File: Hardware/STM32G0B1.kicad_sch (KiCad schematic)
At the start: 20 parts, among them SW1 SW_Push, SW2 SW_Push, SW3 SW_Push, SW4 SW_Push, SW5 SW_Push

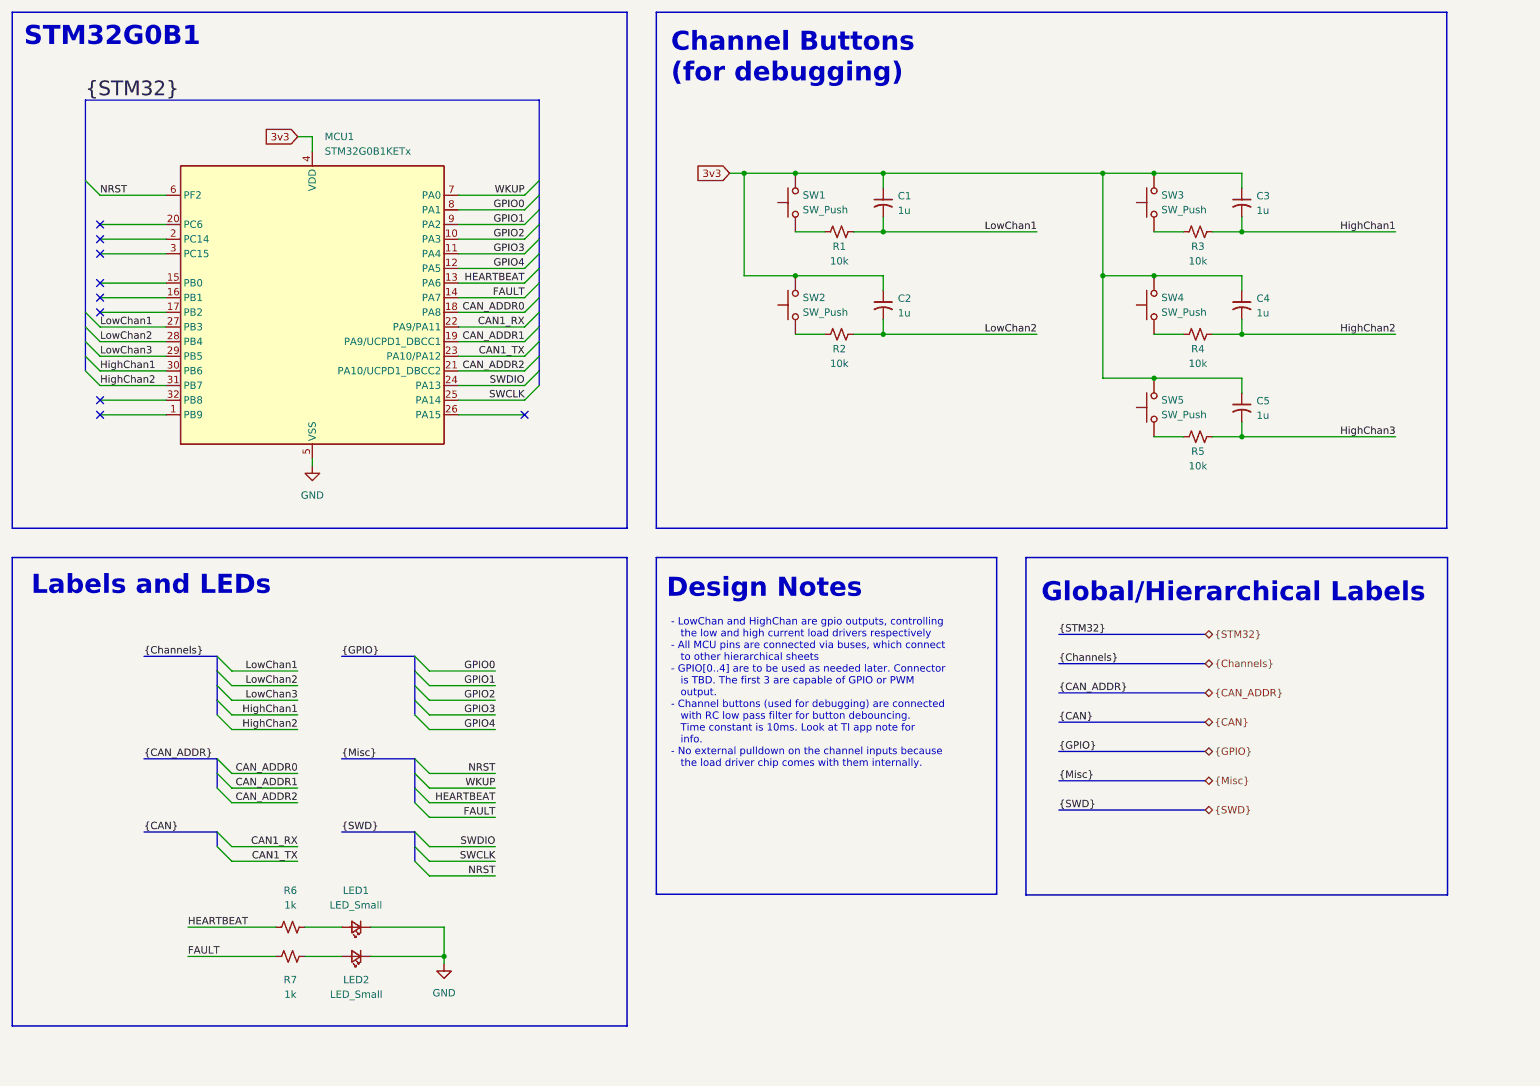
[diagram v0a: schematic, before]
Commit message: Finished the ISOW1044 Schematic
- Ported over Kostadin's schematic

Co-authored-by: Kostadin Madjovski <155325994+bivein@users.noreply.github.com>
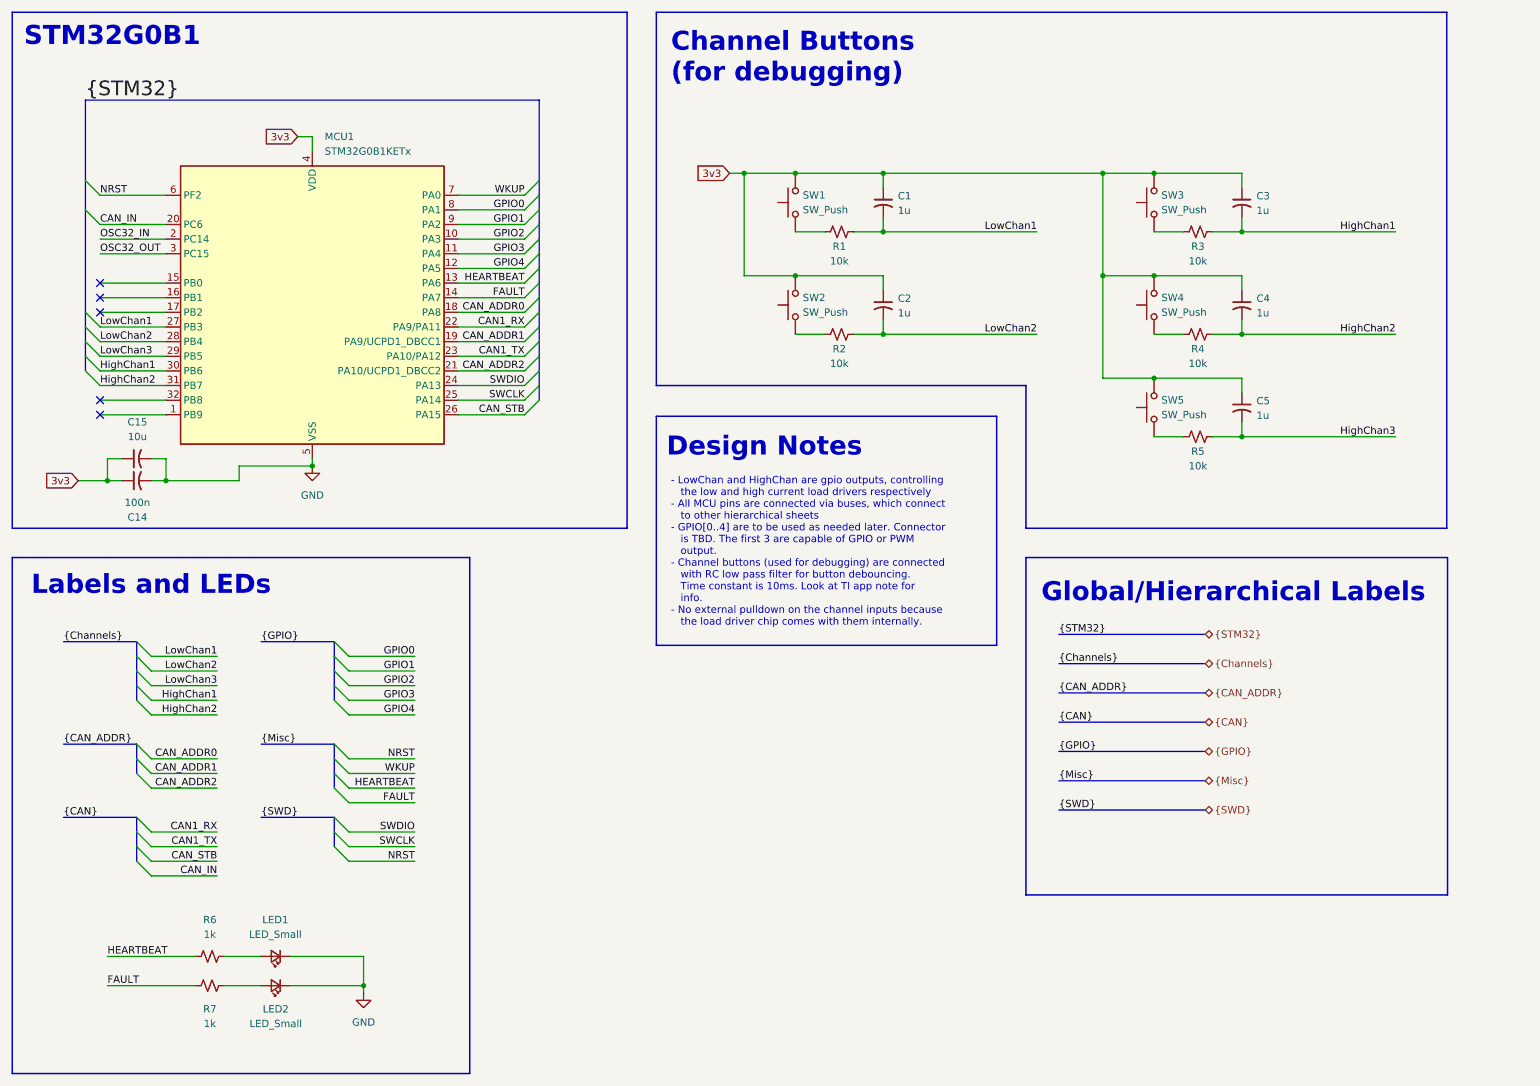
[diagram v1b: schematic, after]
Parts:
- added C14: 100n, symbol Device:C_Small_US
- added C15: 10u, symbol Device:C_Small_US
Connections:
- net 3v3: now also C14.1, C15.1
- net GND: now also C14.2, C15.2
- net OSC32_IN: now reaches MCU1.2 (PC14)
- net CAN_IN: now reaches MCU1.20 (PC6)
- net CAN_STB: now reaches MCU1.26 (PA15)
- net OSC32_OUT: now reaches MCU1.3 (PC15)
- no-connect marks 9 -> 5
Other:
- moved on the sheet: LED1, LED2, R6, R7

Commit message: Finished final touches on schematic.
- Schematic is complete (NOT yet checked by Yassa/Val)
- ERC check is complete, understandable errors excused w/ comments
- Final schematic formatting complete

Co-authored-by: Kostadin Madjovski <155325994+bivein@users.noreply.github.com>
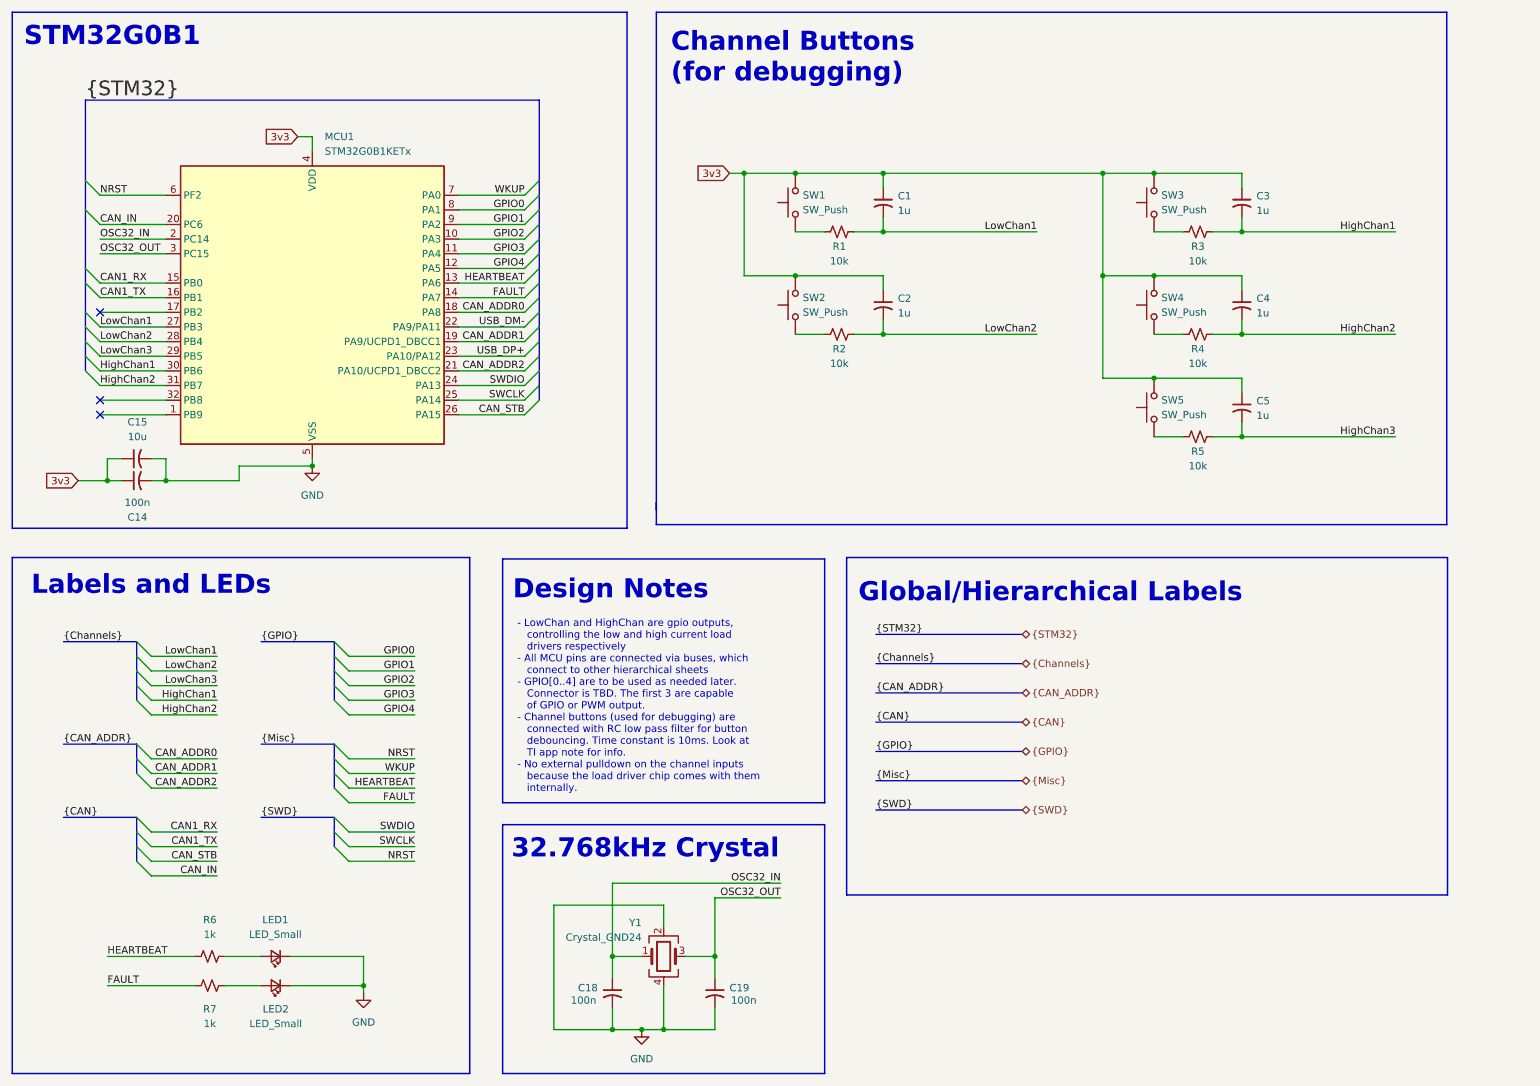
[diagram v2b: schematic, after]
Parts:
- added C18, C19: 100n, symbol Device:C_Small_US
- added Y1: Crystal_GND24, symbol Device:Crystal_GND24
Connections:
- net CAN1_RX: now also MCU1.15 (PB0); no longer MCU1.22 (PA9/PA11)
- net CAN1_TX: now also MCU1.16 (PB1); no longer MCU1.23 (PA10/PA12)
- net GND: now also C18.2, C19.2, Y1.2, Y1.4
- net OSC32_IN: now also C18.1, Y1.1
- net OSC32_OUT: now also C19.1, Y1.3
- new net USB_DM-: MCU1.22 (PA9/PA11)
- new net USB_DP+: MCU1.23 (PA10/PA12)
- no-connect marks 5 -> 3
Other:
- note added: "32.768kHz Crystal"
- company: (none) -> NJIT Solar Car
- title: (none) -> CAN IO Board | STM32G0B1
